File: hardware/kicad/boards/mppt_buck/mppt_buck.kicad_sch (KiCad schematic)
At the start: 20 parts, among them J1 PV ind, J2 lager ud (5V), J3 PWM (Arduino), J4 drive +15V, Q1 IRF530, U1 CNY17, U2 IR2110

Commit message: Assign G/D/S TO-220 footprint to Q_NMOS MOSFETs across boards (match symbol pins)
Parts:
- Q1: footprint energy_system:TO-220-3_Vertical_LaserPads -> energy_system:TO-220-3_Vertical_LaserPads_GDS

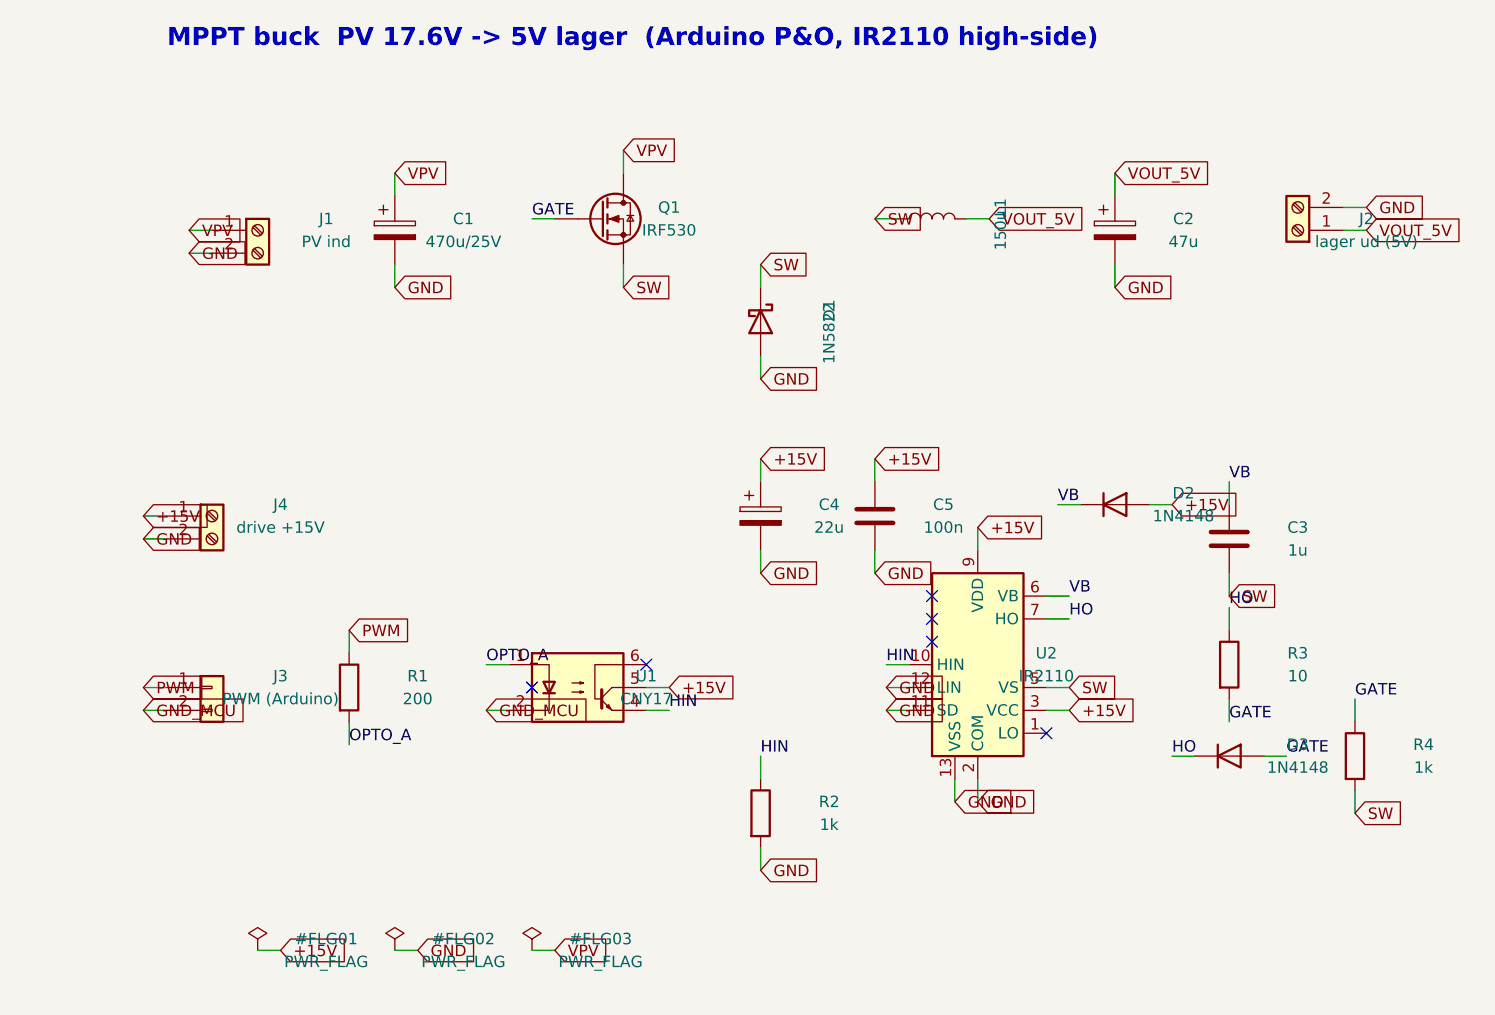
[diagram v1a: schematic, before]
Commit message: system PCB: lock double-sided CNC integration (Phase 0-2.2)
Set up the whole-system board as one double-sided CNC-milled PCB.

- system.kicad_pro: CNC double-sided netclass (clearance 1.0 mm, track 1.0 mm,
  hand-stitch via 2.4/1.0 mm) replacing the laser 0.8 mm rules
- interface contract (docs/superpowers/specs/2026-06-27-...) + rewritten
  label howto for the 5-board split-MCU integration
- split MCU: Arduino owns MPPT (PV INA219 + drives mppt_buck PWM at 5 V),
  C2000 runs motor-buck + boost PID; the two MCUs are fully independent
- current_sense (discrete) dropped; current sensing via PV INA219
- c2000_feedback: strip I-channels + PWM pass, keep 3 V-dividers
  (V1/LOAD/STORE -> ADC)
- hierarchical labels placed on the 5 boards (motor_power, motor_feedback,
  mppt_buck, boost_v2_mill, c2000_feedback) for the system top sheet
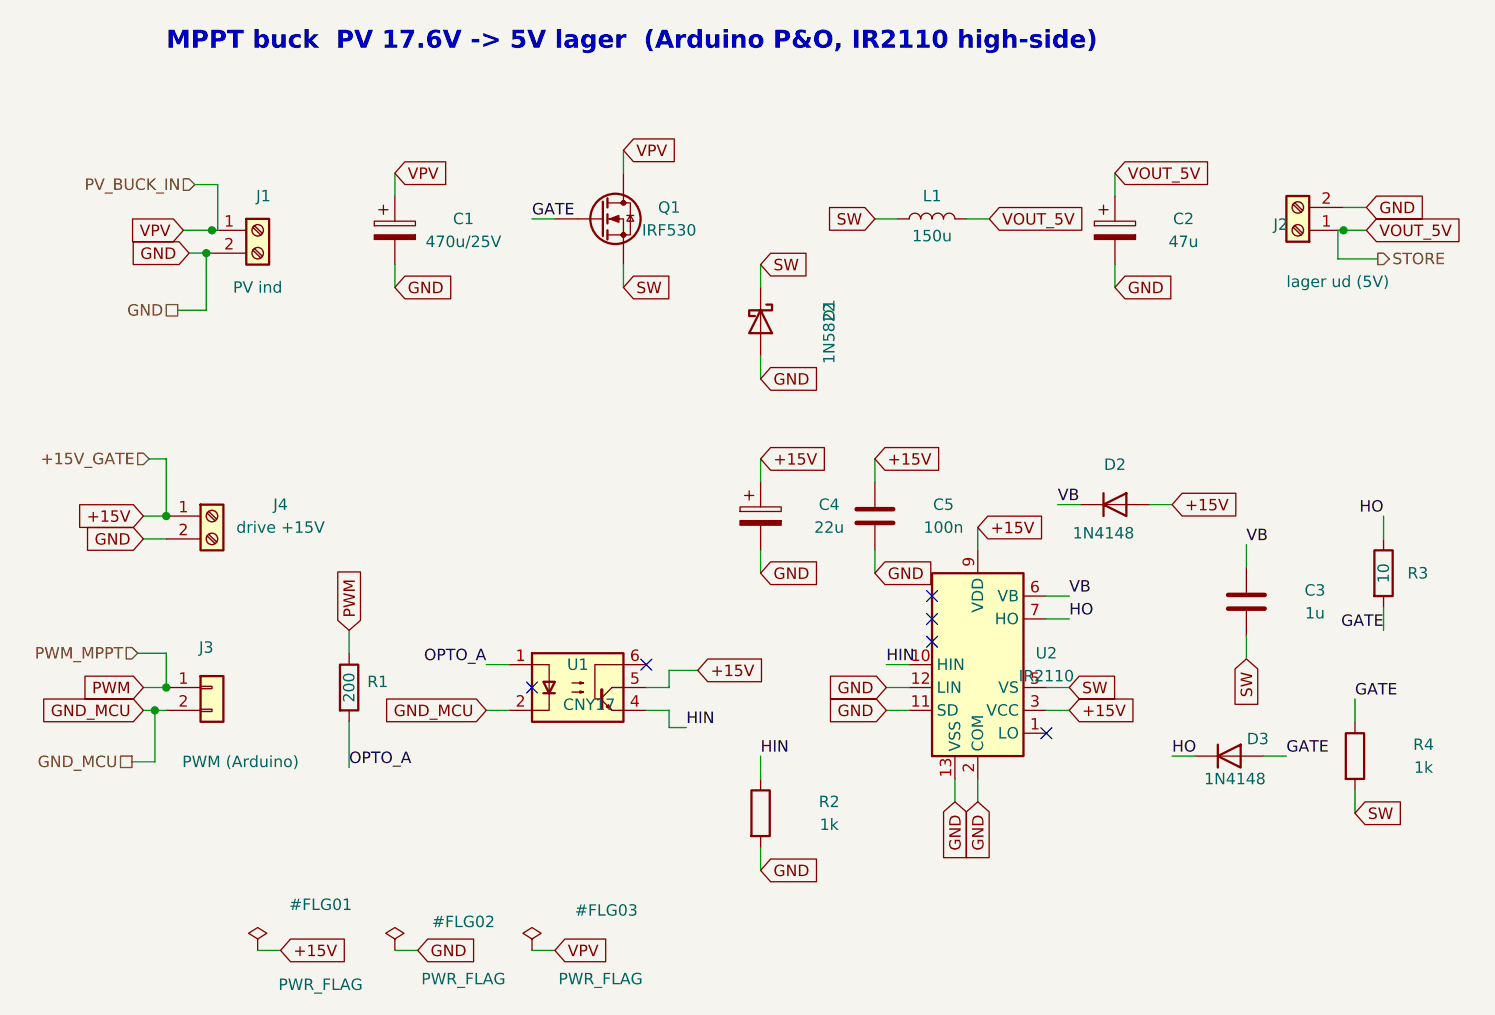
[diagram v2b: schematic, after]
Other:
- moved on the sheet: C3, R3

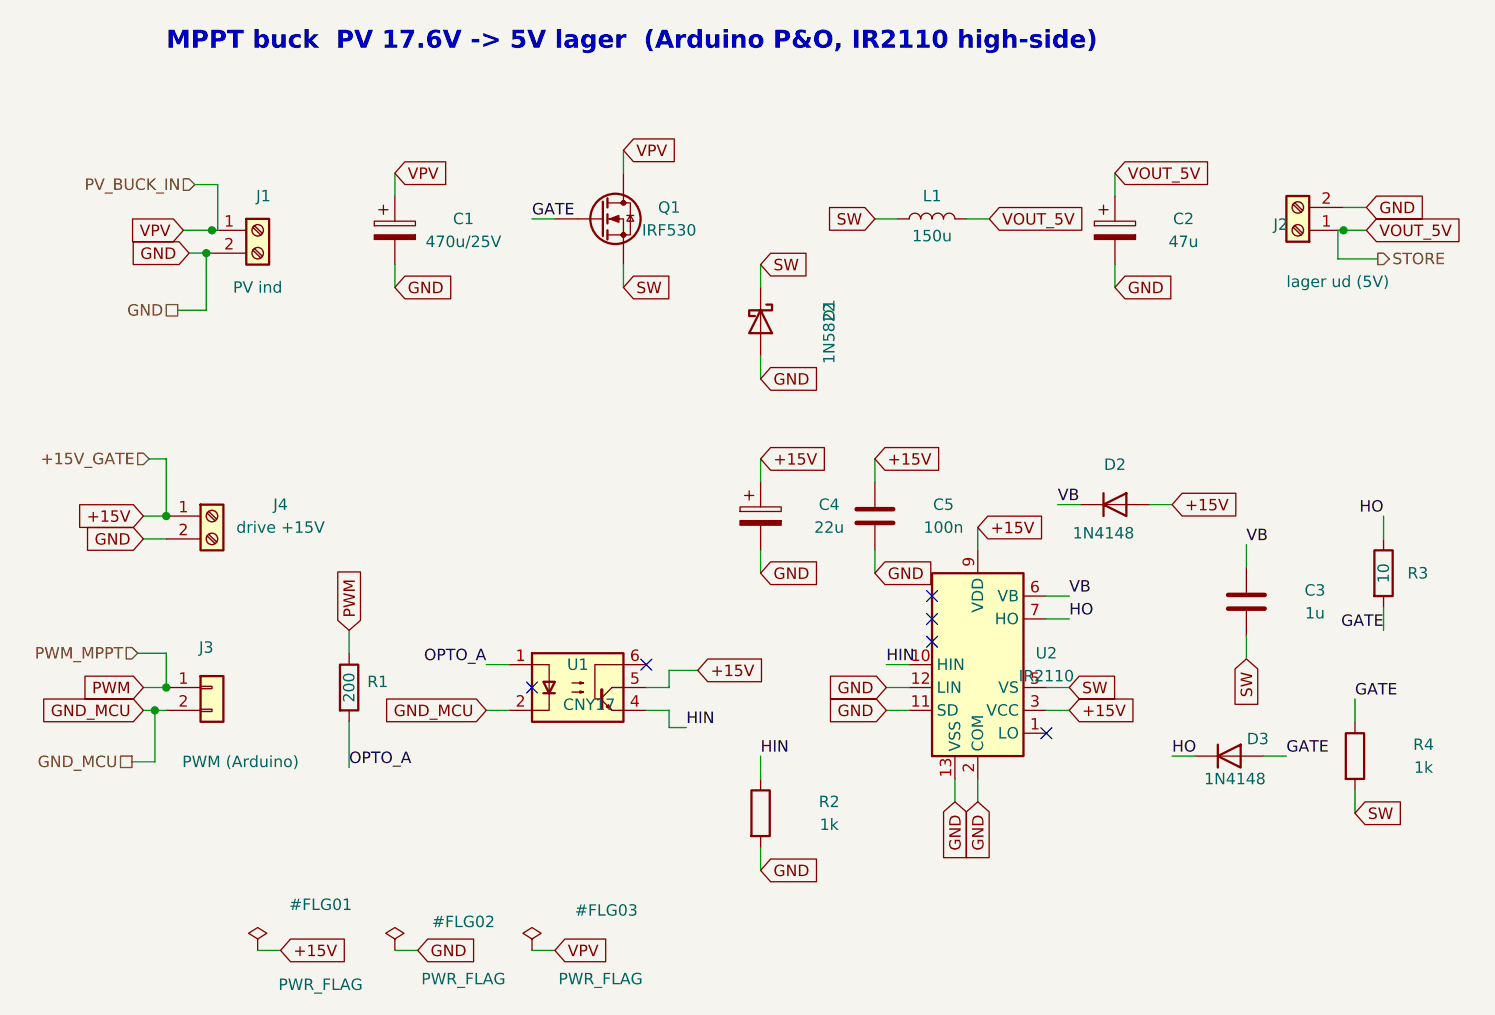
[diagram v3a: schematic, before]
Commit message: system: single edge-connector set + integrated board
- delete 22 redundant board-level I/O connectors (J201-207, J301-302,
  J401-404, J501-504, J601-605); on the monolithic board these are internal
  board-to-board nets (now copper traces) or duplicates of the top-level edge
  set. Nets carried by the hierarchical sheet pins; netlist re-verified.
- C212: real capacitor footprint, + on V1 (was a swap terminal)
- motor_feedback MCU-side powered from +5V_PWR (merged +5V_MCU)
- footprints assigned to all top-level connectors/probes (J_*, TP, R_STAR)
- system.kicad_pcb: integrated board pulled via Update-PCB-from-Schematic
- placement guide (PNG + PDF) + generator/patch scripts
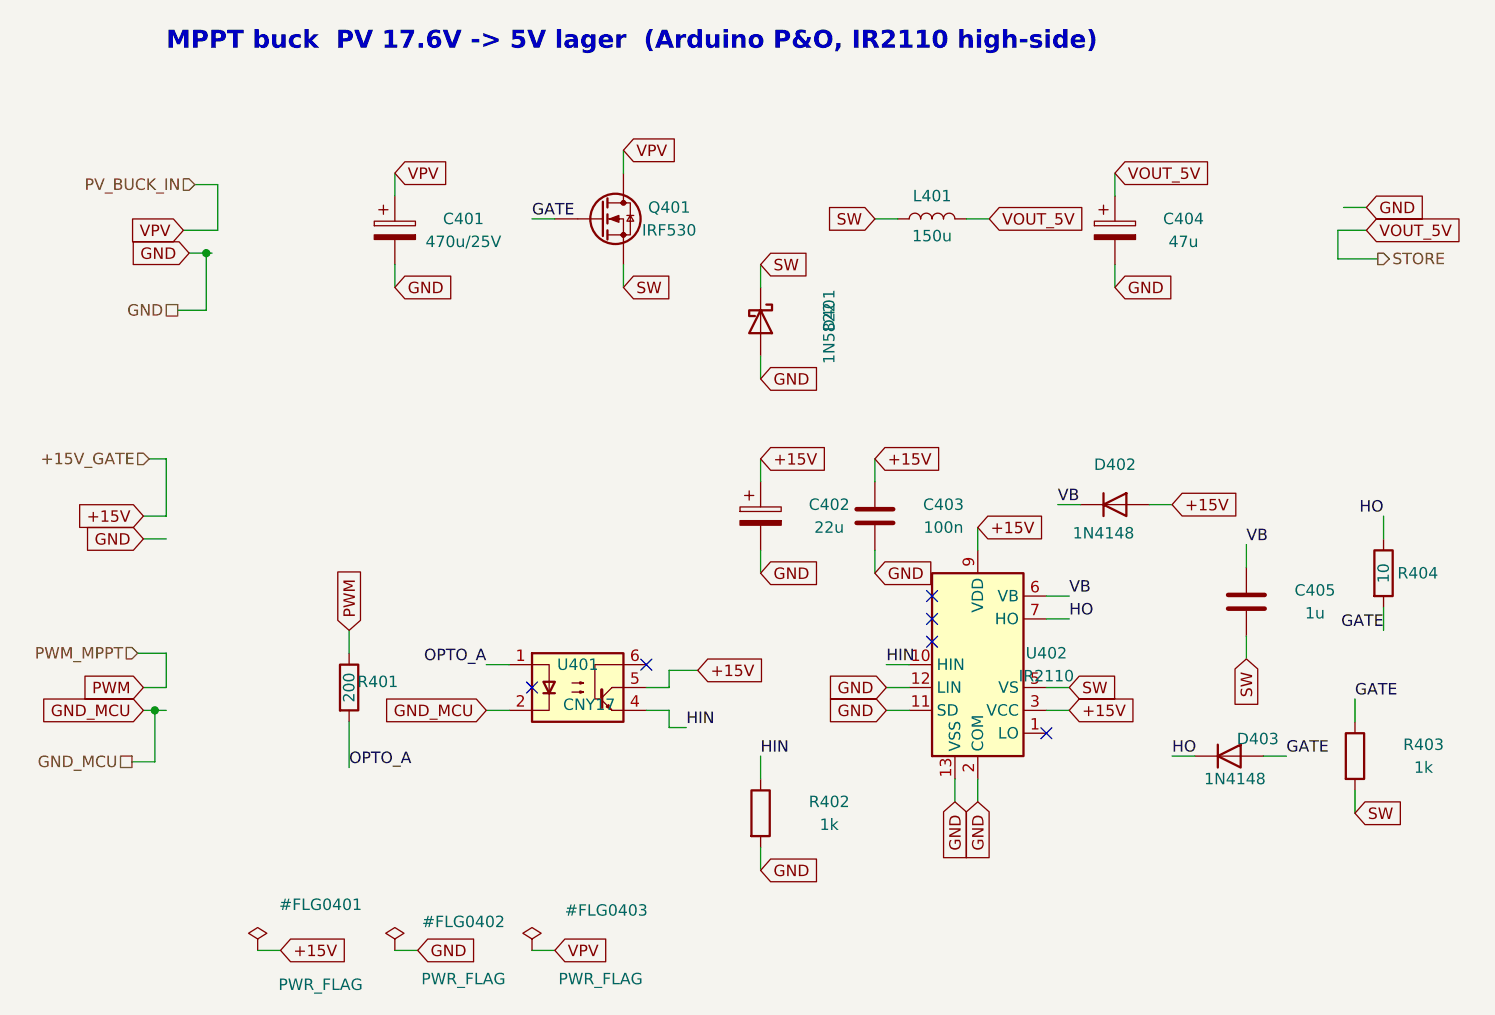
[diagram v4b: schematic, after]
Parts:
- removed J1: PV ind, TerminalBlock:TerminalBlock_bornier-2_P5.08mm, symbol Connector:Screw_Terminal_01x02
- removed J2: lager ud (5V), TerminalBlock:TerminalBlock_bornier-2_P5.08mm, symbol Connector:Screw_Terminal_01x02
- removed J3: PWM (Arduino), Connector_PinHeader_2.54mm:PinHeader_1x02_P2.54mm_Vertical, symbol Connector_Generic:Conn_01x02
- removed J4: drive +15V, TerminalBlock:TerminalBlock_bornier-2_P5.08mm, symbol Connector:Screw_Terminal_01x02
- renumbered C1 to C401, C4 to C402, C5 to C403, C2 to C404, C3 to C405, D1 to D401, D2 to D402, D3 to D403, L1 to L401, Q1 to Q401, R1 to R401, R2 to R402, R4 to R403, R3 to R404, U1 to U401, U2 to U402
